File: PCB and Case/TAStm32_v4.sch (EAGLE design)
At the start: 55 parts, among them CN1 330pF, CN2 330pF, CN3 330pF, CN4 330pF, IC1 74LVC3G17DP, IC2 74LVC3G17DP, IC3 74AXP4T245, IC4 74AXP4T245, J1 ZX62D-B-5PA8, J10 RJSSE538002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

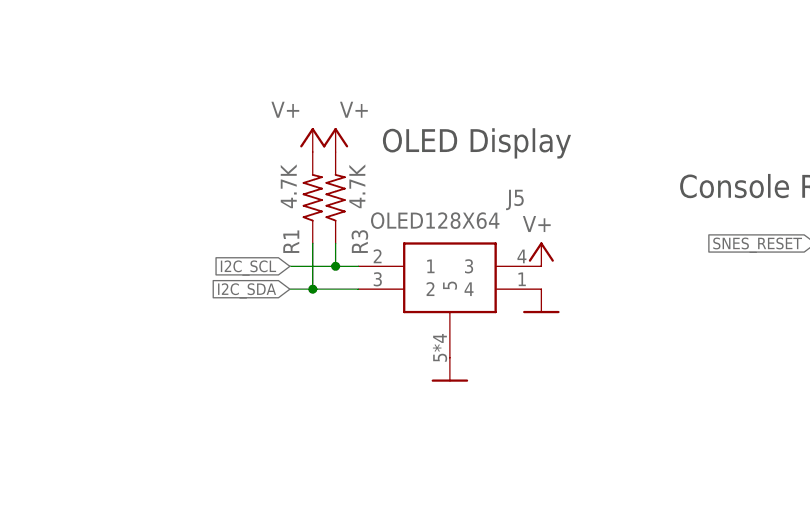
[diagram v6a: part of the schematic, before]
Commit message: fixed OLED pinout
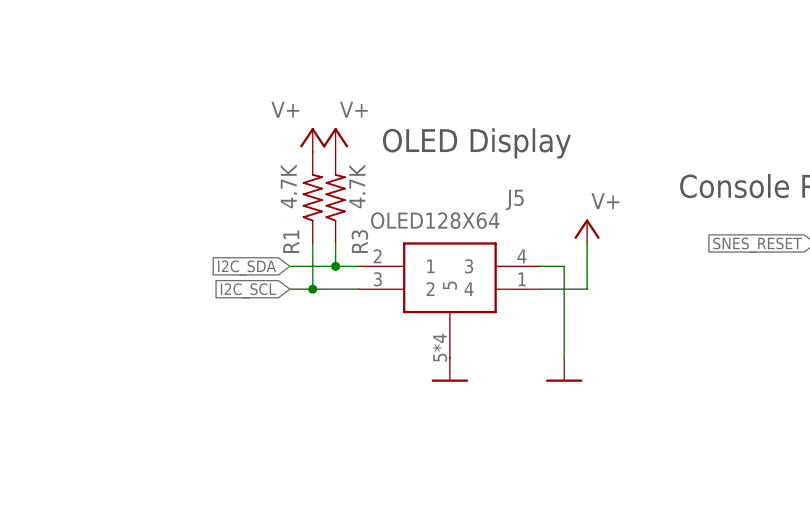
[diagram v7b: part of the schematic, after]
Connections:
- net GND: now also J5.3; no longer J5.4
- net I2C_SCL: now also J5.2, R1.1; no longer J5.1, R3.1
- net I2C_SDA: now also J5.1, R3.1; no longer J5.2, R1.1
- net V+: now also J5.4; no longer J5.3
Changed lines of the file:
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@@
 <part name="C12" library="rcl" library_urn="urn:adsk.eagle:library:334" deviceset="C-EU" device="C0603K" package3d_urn="urn:adsk.eagle:package:23680/2" value="1uF"/>
 <part name="SUPPLY1" library="supply2" library_urn="urn:adsk.eagle:library:372" deviceset="V+" device=""/>
-<part name="SUPPLY2" library="supply2" library_urn="urn:adsk.eagle:library:372" deviceset="V+" device=""/>
 <part name="GND14" library="supply1" library_urn="urn:adsk.eagle:library:371" deviceset="GND" device=""/>
 <part name="GND15" library="supply1" library_urn="urn:adsk.eagle:library:371" deviceset="GND" device=""/>
-<part name="GND5" library="supply1" library_urn="urn:adsk.eagle:library:371" deviceset="GND" device=""/>
 <part name="SUPPLY7" library="supply2" library_urn="urn:adsk.eagle:library:372" deviceset="+5V" device=""/>
 <part name="U1" library="STM32F446RET6" deviceset="STM32F446RET7" device="" package3d_urn="urn:adsk.eagle:package:18856813/2" value="STM32F446RET6"/>
@@
 <part name="S2" library="TAStm32_v4" deviceset="3-1825910-1_SWITCHN" device=""/>
 <part name="S1" library="TAStm32_v4" deviceset="3-1825910-1_SWITCHN" device=""/>
-<part name="S4" library="TAStm32_v4" deviceset="3-1825910-1_SWITCHN" device=""/>
+<part name="S4" library="TAStm32_v4" deviceset="3-1825910-1_SWITCHN" device="" override_package3d_urn="urn:adsk.eagle:package:29257505/2" override_package_urn="urn:adsk.eagle:footprint:29257506/1"/>
 <part name="S3" library="TAStm32_v4" deviceset="3-1825910-1_SWITCHN" device=""/>
+<part name="SUPPLY2" library="supply2" library_urn="urn:adsk.eagle:library:372" deviceset="V+" device=""/>
+<part name="GND5" library="supply1" library_urn="urn:adsk.eagle:library:371" deviceset="GND" device=""/>
 </parts>
 <sheets>
@@
 <attribute name="VALUE" x="115.57" y="196.85" size="1.778" layer="96"/>
 </instance>
-<instance part="SUPPLY2" gate="1" x="320.04" y="48.26" smashed="yes" rot="MR0">
-<attribute name="VALUE" x="321.31" y="49.53" size="1.778" layer="96" rot="MR0"/>
-</instance>
 <instance part="GND14" gate="1" x="99.06" y="218.44" smashed="yes"/>
 <instance part="GND15" gate="1" x="124.46" y="218.44" smashed="yes"/>
-<instance part="GND5" gate="1" x="320.04" y="40.64" smashed="yes" rot="MR0"/>
 <instance part="SUPPLY7" gate="+5V" x="124.46" y="231.14" smashed="yes">
 <attribute name="VALUE" x="122.555" y="234.315" size="1.778" layer="96"/>
@@
 <attribute name="VALUE" x="115.57" y="91.44" size="1.778" layer="96" align="center-left"/>
 </instance>
+<instance part="SUPPLY2" gate="1" x="325.12" y="50.8" smashed="yes" rot="MR0">
+<attribute name="VALUE" x="328.93" y="52.07" size="1.778" layer="96" rot="MR0"/>
+</instance>
+<instance part="GND5" gate="1" x="322.58" y="33.02" smashed="yes" rot="MR0"/>
 </instances>
 <busses>
@@
 </segment>
 <segment>
-<pinref part="GND5" gate="1" pin="GND"/>
-<pinref part="J5" gate="G$1" pin="4"/>
-</segment>
-<segment>
 <pinref part="GND9" gate="1" pin="GND"/>
 <pinref part="J5" gate="G$1" pin="5"/>
@@
 <junction x="241.3" y="71.12"/>
 <wire x1="243.84" y1="71.12" x2="236.22" y2="71.12" width="0.1524" layer="91"/>
+</segment>
+<segment>
+<pinref part="GND5" gate="1" pin="GND"/>
+<wire x1="322.58" y1="35.56" x2="322.58" y2="45.72" width="0.1524" layer="91"/>
+<pinref part="J5" gate="G$1" pin="3"/>
+<wire x1="322.58" y1="45.72" x2="320.04" y2="45.72" width="0.1524" layer="91"/>
 </segment>
 </net>
@@
 </segment>
 <segment>
-<pinref part="SUPPLY2" gate="1" pin="V+"/>
-<pinref part="J5" gate="G$1" pin="3"/>
-</segment>
-<segment>
 <pinref part="SUPPLY6" gate="1" pin="V+"/>
 <pinref part="J3" gate="A" pin="1"/>
@@
 <wire x1="185.42" y1="68.58" x2="185.42" y2="66.04" width="0.1524" layer="91"/>
 </segment>
+<segment>
+<pinref part="J5" gate="G$1" pin="4"/>
+<pinref part="SUPPLY2" gate="1" pin="V+"/>
+<wire x1="320.04" y1="43.18" x2="325.12" y2="43.18" width="0.1524" layer="91"/>
+<wire x1="325.12" y1="43.18" x2="325.12" y2="48.26" width="0.1524" layer="91"/>
+</segment>
 </net>
 <net name="I2C_SCL" class="0">
+<segment>
+<wire x1="45.72" y1="101.6" x2="43.18" y2="101.6" width="0.1524" layer="91"/>
+<label x="43.18" y="101.6" size="1.27" layer="95" rot="R180" xref="yes"/>
+<pinref part="U1" gate="G$1" pin="PB8"/>
+</segment>
+<segment>
+<label x="292.1" y="43.18" size="1.27" layer="95" rot="MR0" xref="yes"/>
+<pinref part="R1" gate="G$1" pin="1"/>
+<wire x1="294.64" y1="43.18" x2="292.1" y2="43.18" width="0.1524" layer="91"/>
+<wire x1="294.64" y1="48.26" x2="294.64" y2="43.18" width="0.1524" layer="91"/>
+<pinref part="J5" gate="G$1" pin="2"/>
+<wire x1="294.64" y1="43.18" x2="299.72" y2="43.18" width="0.1524" layer="91"/>
+<junction x="294.64" y="43.18"/>
+</segment>
+</net>
+<net name="I2C_SDA" class="0">
+<segment>
+<wire x1="45.72" y1="99.06" x2="43.18" y2="99.06" width="0.1524" layer="91"/>
+<label x="43.18" y="99.06" size="1.27" layer="95" rot="R180" xref="yes"/>
+<pinref part="U1" gate="G$1" pin="PB9"/>
+</segment>
 <segment>
 <label x="292.1" y="45.72" size="1.27" layer="95" rot="MR0" xref="yes"/>
@@
 <junction x="297.18" y="45.72"/>
 </segment>
-<segment>
-<wire x1="45.72" y1="101.6" x2="43.18" y2="101.6" width="0.1524" layer="91"/>
-<label x="43.18" y="101.6" size="1.27" layer="95" rot="R180" xref="yes"/>
-<pinref part="U1" gate="G$1" pin="PB8"/>
-</segment>
-</net>
-<net name="I2C_SDA" class="0">
-<segment>
-<label x="292.1" y="43.18" size="1.27" layer="95" rot="MR0" xref="yes"/>
-<pinref part="R1" gate="G$1" pin="1"/>
-<wire x1="294.64" y1="43.18" x2="292.1" y2="43.18" width="0.1524" layer="91"/>
-<wire x1="294.64" y1="48.26" x2="294.64" y2="43.18" width="0.1524" layer="91"/>
-<pinref part="J5" gate="G$1" pin="2"/>
-<wire x1="294.64" y1="43.18" x2="299.72" y2="43.18" width="0.1524" layer="91"/>
-<junction x="294.64" y="43.18"/>
-</segment>
-<segment>
-<wire x1="45.72" y1="99.06" x2="43.18" y2="99.06" width="0.1524" layer="91"/>
-<label x="43.18" y="99.06" size="1.27" layer="95" rot="R180" xref="yes"/>
-<pinref part="U1" gate="G$1" pin="PB9"/>
-</segment>
-</net>
+</net>

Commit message: 3D parts
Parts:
- C1, C10, C11, C12, C13, C14, C15, C16, C17, C2, C3, C4, C5, C6, C7, C8, C9: device rcl:C-EUC0603K -> TAStm32_v4:C-EUC0603K
- CN1, CN2, CN3, CN4: device SamacSys_Parts:CA0612KRX7R7BB104 -> TAStm32_v4:CA0612KRX7R7BB104
- IC1, IC2: device SamacSys_Parts:74HCT3G07DP-Q100H -> TAStm32_v4:74HCT3G07DP-Q100H
- IC3, IC4: device SamacSys_Parts:74AVCH4T245PW,118 -> TAStm32_v4:74AVCH4T245PW,118
- J1: device ZX62D-B-5PA8:ZX62D-B-5PA8 -> TAStm32_v4:ZX62D-B-5PA8
- J12: device SOICbite_Eagle:SOICBITE -> TAStm32_v4:SOICBITE
- J2: device SamacSys_Parts:UE27-AC54-100 -> TAStm32_v4:UE27-AC54-100
- J3: device TSM-105-02-L-SH:TSM-105-02-L-SHJ -> TAStm32_v4:TSM-105-02-L-SHJ
- J6, J7: device SAMTEC-TSM-116-01-X-SV:SAMTEC-TSM-116-01-X-SVJ -> TAStm32_v4:SAMTEC-TSM-116-01-X-SVJ
- R1, R2, R3: device rcl:R-US_R0805 -> TAStm32_v4:R-US_R0805
- RN1, RN2, RN3, RN4, RN5, RN7: device resistor-net:CTS742C083 -> TAStm32_v4:CTS742C083
- U1: device STM32F446RET6:STM32F446RET7 -> TAStm32_v4:STM32F446RET7
- U2: device linear:MC33269ST-3.3T3 -> TAStm32_v4:MC33269ST-3.3T3
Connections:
- net GND: now also J5.1; no longer J5.3
- net I2C_SDA: now also J5.3; no longer J5.1
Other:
- moved on the sheet: J5, R1, R3
